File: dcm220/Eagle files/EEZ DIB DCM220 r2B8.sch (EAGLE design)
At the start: 244 parts, among them IC1 Si8662AB-B-IS1, IC10 MC33272ADR2G, IC11 LT3763EFE#PBF, IC12 MC33274ADR2G, IC13 LT3763EFE#PBF, IC2 TPS54060DGQ, IC3 Si8641AB-B-IS1, IC4 M24C32-WMN6P, IC5 LP2985-33DBVR, IC6 74HC2G04GW,125, IC7 N.C., IC8 STM32F373C8T6, IC9 TL431B, J1 4907, J2 571-0500, J3 571-0100, J4 571-0500, J5 571-0100, Q1 BSP716NH6327XTSA1, Q10 BSS84, Q2 NTD5867NLT4G, Q3 NTD5867NLT4G, Q4 BSS205NH6327XTSA1, Q5 BSS84, Q6 BSP716NH6327XTSA1, Q7 NTD5867NLT4G, Q8 NTD5867NLT4G, Q9 BSS205NH6327XTSA1, X1 39-30-1020, X2 77317-104-28LF, X3 N.C., X4 DS1024-2*5R0, Y1 LF XTAL026392

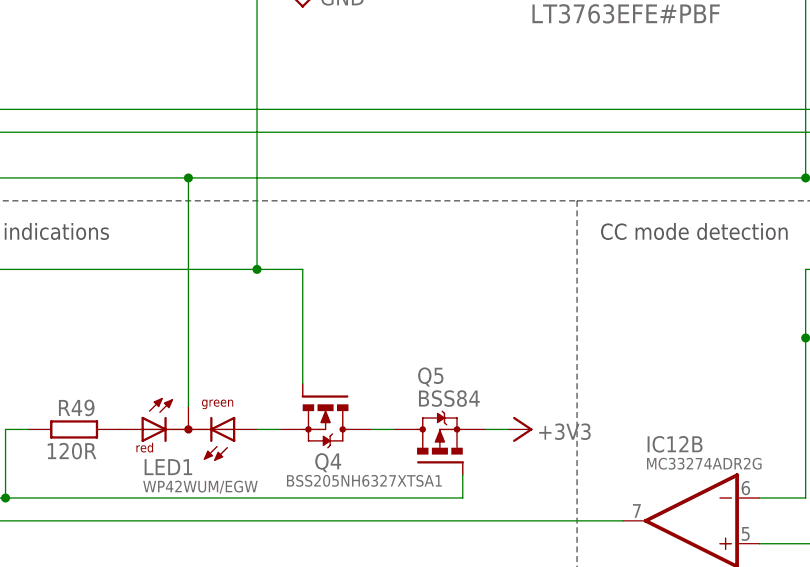
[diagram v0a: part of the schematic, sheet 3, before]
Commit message: DCM220 OE pull-down added
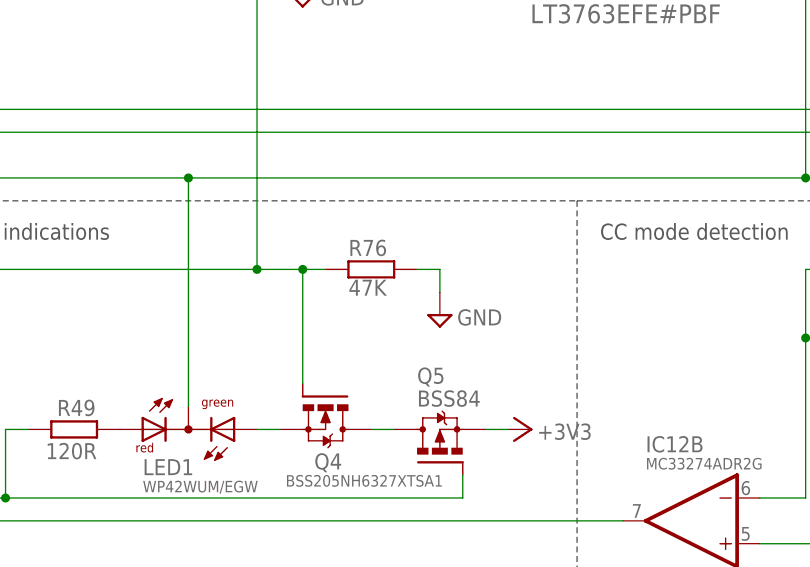
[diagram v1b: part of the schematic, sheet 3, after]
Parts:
- added R76, R77: 47K, rcl:R-EU_R0805
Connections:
- net GND: now also R76.2, R77.2
- net OE#1: now also R76.1
- net OE#2: now also R77.1
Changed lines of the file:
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@@
 <setting verticaltext="up"/>
 </settings>
-<grid distance="0.025" unitdist="inch" unit="inch" style="lines" multiple="4" display="no" altdistance="0.01" altunitdist="inch" altunit="inch"/>
+<grid distance="0.1" unitdist="inch" unit="inch" style="lines" multiple="1" display="no" altdistance="0.01" altunitdist="inch" altunit="inch"/>
 <layers>
 <layer number="1" name="Top" color="4" fill="1" visible="no" active="no"/>
@@
 <part name="+3V15" library="supply1" deviceset="+3V3" device=""/>
 <part name="U$3" library="OSHWA" deviceset="CERT" device="-SMALL" value="HR000002"/>
+<part name="R76" library="rcl" deviceset="R-EU_" device="R0805" value="47K"/>
+<part name="SUPPLY6" library="supply2" deviceset="GND" device=""/>
+<part name="R77" library="rcl" deviceset="R-EU_" device="R0805" value="47K"/>
+<part name="SUPPLY45" library="supply2" deviceset="GND" device=""/>
 </parts>
 <sheets>
@@
 <attribute name="VALUE" x="242.57" y="151.13" size="1.778" layer="96"/>
 </instance>
+<instance part="R76" gate="G$1" x="58.42" y="50.8" smashed="yes" rot="MR180">
+<attribute name="NAME" x="55.88" y="52.2986" size="1.778" layer="95"/>
+<attribute name="VALUE" x="55.88" y="49.657" size="1.778" layer="96" rot="MR180"/>
+</instance>
+<instance part="SUPPLY6" gate="GND" x="66.04" y="45.72" smashed="yes">
+<attribute name="VALUE" x="67.945" y="46.355" size="1.778" layer="96" rot="MR180"/>
+</instance>
 </instances>
 <busses>
@@
 <pinref part="SUPPLY44" gate="GND" pin="GND"/>
 </segment>
+<segment>
+<pinref part="R76" gate="G$1" pin="2"/>
+<wire x1="63.5" y1="50.8" x2="66.04" y2="50.8" width="0.1524" layer="91"/>
+<wire x1="66.04" y1="50.8" x2="66.04" y2="48.26" width="0.1524" layer="91"/>
+<pinref part="SUPPLY6" gate="GND" pin="GND"/>
+</segment>
 </net>
 <net name="OE#1" class="0">
@@
 <wire x1="45.72" y1="50.8" x2="50.8" y2="50.8" width="0.1524" layer="91"/>
 <wire x1="50.8" y1="50.8" x2="50.8" y2="38.1" width="0.1524" layer="91"/>
+<pinref part="R76" gate="G$1" pin="1"/>
+<wire x1="53.34" y1="50.8" x2="50.8" y2="50.8" width="0.1524" layer="91"/>
+<junction x="50.8" y="50.8"/>
 </segment>
 </net>
@@
 <attribute name="VALUE" x="113.284" y="159.639" size="1.778" layer="96" rot="MR180"/>
 </instance>
+<instance part="R77" gate="G$1" x="58.42" y="50.8" smashed="yes" rot="MR180">
+<attribute name="NAME" x="55.88" y="52.2986" size="1.778" layer="95"/>
+<attribute name="VALUE" x="55.88" y="49.657" size="1.778" layer="96" rot="MR180"/>
+</instance>
+<instance part="SUPPLY45" gate="GND" x="66.04" y="45.72" smashed="yes">
+<attribute name="VALUE" x="67.945" y="46.355" size="1.778" layer="96" rot="MR180"/>
+</instance>
 </instances>
 <busses>
@@
 <pinref part="SUPPLY19" gate="GND" pin="GND"/>
 </segment>
+<segment>
+<pinref part="R77" gate="G$1" pin="2"/>
+<wire x1="63.5" y1="50.8" x2="66.04" y2="50.8" width="0.1524" layer="91"/>
+<wire x1="66.04" y1="50.8" x2="66.04" y2="48.26" width="0.1524" layer="91"/>
+<pinref part="SUPPLY45" gate="GND" pin="GND"/>
+</segment>
 </net>
 <net name="N$28" class="0">
@@
 <wire x1="45.72" y1="137.16" x2="45.72" y2="50.8" width="0.1524" layer="91"/>
 <junction x="45.72" y="50.8"/>
+<wire x1="53.34" y1="50.8" x2="50.8" y2="50.8" width="0.1524" layer="91"/>
+<junction x="50.8" y="50.8"/>
+<pinref part="R77" gate="G$1" pin="1"/>
 </segment>
 </net>

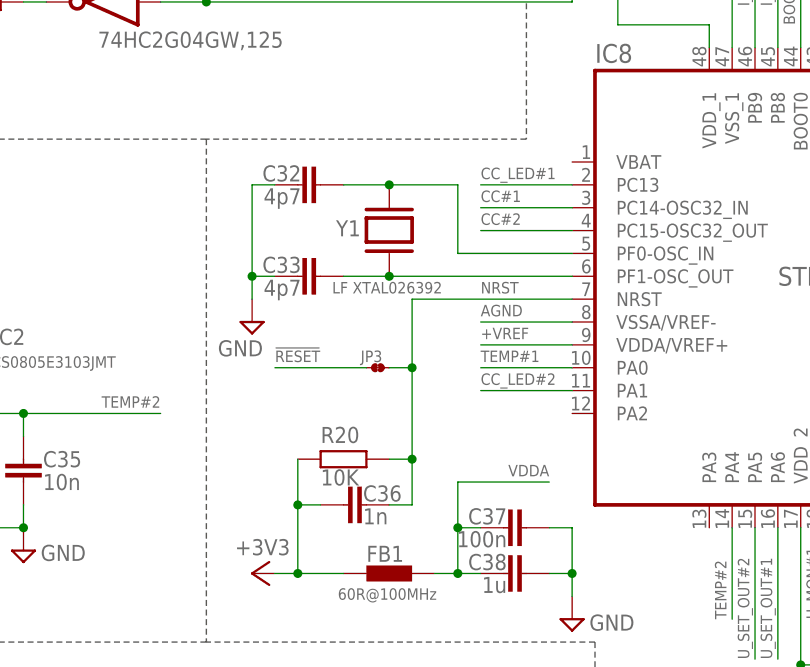
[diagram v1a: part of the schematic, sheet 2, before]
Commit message: DCM220 HSE removed
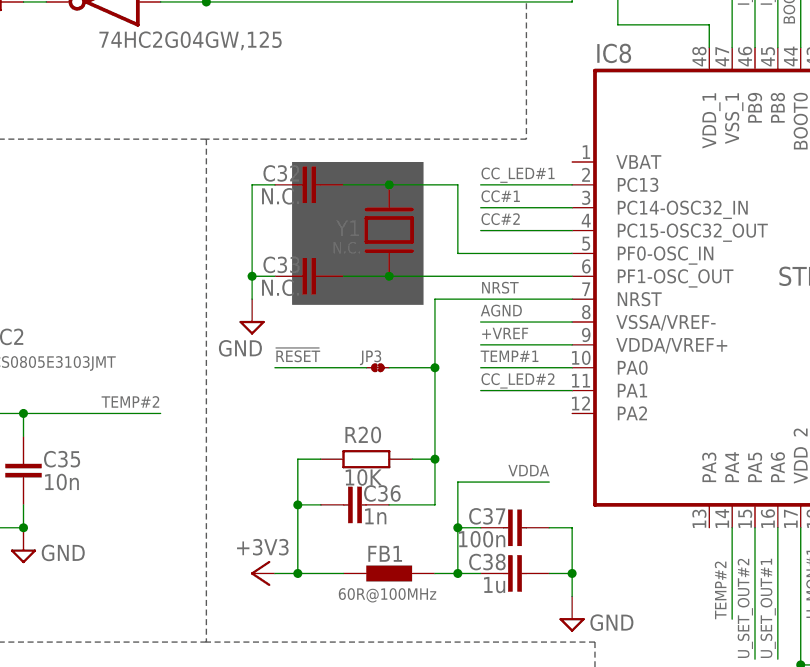
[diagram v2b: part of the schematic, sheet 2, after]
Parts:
- C32, C33: value 4p7 -> N.C.
- Y1: value LF XTAL026392 -> N.C.
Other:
- moved on the sheet: R20
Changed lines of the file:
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@@
 <part name="C62" library="EEZ_Lib1" deviceset="ECAP" device="5G_10.5MM" value="UVZ1E102MPD"/>
 <part name="C82" library="EEZ_Lib1" deviceset="ECAP" device="5G_10.5MM" value="UVZ1E102MPD"/>
-<part name="Y1" library="EEZ_Lib1" deviceset="XTAL" device="7.5X5.1-B" value="LF XTAL026392"/>
-<part name="C32" library="rcl" deviceset="C-EU" device="C0603" value="4p7"/>
-<part name="C33" library="rcl" deviceset="C-EU" device="C0603" value="4p7"/>
+<part name="Y1" library="EEZ_Lib1" deviceset="XTAL" device="7.5X5.1-B" value="N.C."/>
+<part name="C32" library="rcl" deviceset="C-EU" device="C0603" value="N.C."/>
+<part name="C33" library="rcl" deviceset="C-EU" device="C0603" value="N.C."/>
 <part name="SUPPLY49" library="supply2" deviceset="GND" device=""/>
 <part name="X4" library="EEZ_connectors" deviceset="SSW-105-02-T-D-RA" device="" value="DS1024-2*5R0"/>
@@
 <wire x1="208.28" y1="38.1" x2="208.28" y2="83.82" width="0.1524" layer="97" style="shortdash"/>
 <text x="210.82" y="78.74" size="1.778" layer="97">Voltage reference</text>
+<rectangle x1="90.805" y1="98.425" x2="105.41" y2="114.3" layer="97"/>
 </plain>
 <instances>
@@
 <instance part="Y1" gate="A" x="101.6" y="106.68" smashed="yes" rot="MR90">
 <attribute name="NAME" x="98.425" y="106.045" size="1.778" layer="95" rot="MR0"/>
-<attribute name="VALUE" x="95.25" y="100.965" size="1.27" layer="96" rot="MR180"/>
+<attribute name="VALUE" x="95.25" y="105.41" size="1.27" layer="96" rot="MR180"/>
 </instance>
 <instance part="C32" gate="G$1" x="91.44" y="111.76" smashed="yes" rot="R90">
@@
 <attribute name="NAME" x="98.425" y="92.075" size="1.27" layer="95"/>
 </instance>
-<instance part="R20" gate="G$1" x="96.52" y="81.28" smashed="yes" rot="MR180">
-<attribute name="NAME" x="93.98" y="84.8614" size="1.778" layer="95" rot="MR180"/>
-<attribute name="VALUE" x="93.98" y="80.137" size="1.778" layer="96" rot="MR180"/>
+<instance part="R20" gate="G$1" x="99.06" y="81.28" smashed="yes" rot="MR180">
+<attribute name="NAME" x="96.52" y="84.8614" size="1.778" layer="95" rot="MR180"/>
+<attribute name="VALUE" x="96.52" y="80.137" size="1.778" layer="96" rot="MR180"/>
 </instance>
 <instance part="C36" gate="G$1" x="99.06" y="76.2" smashed="yes" rot="MR90">
@@
 <junction x="91.44" y="68.58"/>
 <pinref part="R20" gate="G$1" pin="1"/>
+<junction x="91.44" y="76.2"/>
+<wire x1="93.98" y1="81.28" x2="91.44" y2="81.28" width="0.1524" layer="91"/>
 <wire x1="91.44" y1="81.28" x2="91.44" y2="76.2" width="0.1524" layer="91"/>
-<junction x="91.44" y="76.2"/>
 </segment>
 <segment>
@@
 <pinref part="IC8" gate="G$1" pin="NRST"/>
 <pinref part="JP3" gate="G$1" pin="2"/>
-<wire x1="121.92" y1="99.06" x2="104.14" y2="99.06" width="0.1524" layer="91"/>
-<wire x1="104.14" y1="99.06" x2="104.14" y2="91.44" width="0.1524" layer="91"/>
-<wire x1="104.14" y1="91.44" x2="101.6" y2="91.44" width="0.1524" layer="91"/>
+<wire x1="121.92" y1="99.06" x2="106.68" y2="99.06" width="0.1524" layer="91"/>
+<wire x1="106.68" y1="99.06" x2="106.68" y2="91.44" width="0.1524" layer="91"/>
+<wire x1="106.68" y1="91.44" x2="101.6" y2="91.44" width="0.1524" layer="91"/>
 <label x="111.76" y="99.695" size="1.27" layer="102"/>
 <pinref part="R20" gate="G$1" pin="2"/>
-<wire x1="101.6" y1="81.28" x2="104.14" y2="81.28" width="0.1524" layer="91"/>
-<wire x1="104.14" y1="81.28" x2="104.14" y2="91.44" width="0.1524" layer="91"/>
-<junction x="104.14" y="91.44"/>
+<wire x1="104.14" y1="81.28" x2="106.68" y2="81.28" width="0.1524" layer="91"/>
+<wire x1="106.68" y1="81.28" x2="106.68" y2="91.44" width="0.1524" layer="91"/>
+<junction x="106.68" y="91.44"/>
 <pinref part="C36" gate="G$1" pin="1"/>
-<wire x1="101.6" y1="76.2" x2="104.14" y2="76.2" width="0.1524" layer="91"/>
-<wire x1="104.14" y1="76.2" x2="104.14" y2="81.28" width="0.1524" layer="91"/>
-<junction x="104.14" y="81.28"/>
-</segment>
-<segment>
+<wire x1="101.6" y1="76.2" x2="106.68" y2="76.2" width="0.1524" layer="91"/>
+<wire x1="106.68" y1="76.2" x2="106.68" y2="81.28" width="0.1524" layer="91"/>
+<junction x="106.68" y="81.28"/>
+</segment>
+<segment>

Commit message: ULVO levels update for power modules
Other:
- note added: "UVLO off: +26.5 V UVLO on: +27.5 V"
- note removed: "UVLO off: +33 V UVLO on: +38 V"
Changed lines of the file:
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@@
 <text x="247.65" y="132.715" size="1.4224" layer="101">28 UART_TX</text>
 <wire x1="71.12" y1="2.54" x2="71.12" y2="60.96" width="0.1524" layer="97" style="shortdash"/>
-<text x="36.83" y="113.665" size="1.778" layer="103">UVLO off: +33 V
-UVLO on: +38 V</text>
+<text x="36.83" y="113.665" size="1.778" layer="103">UVLO off: +26.5 V
+UVLO on: +27.5 V</text>
 <text x="76.2" y="58.42" size="1.778" layer="97" rot="MR180">+3V3 LDO</text>
 <text x="193.675" y="81.28" size="1.27" layer="103">Max. transfer speed is 1MBit/s</text>

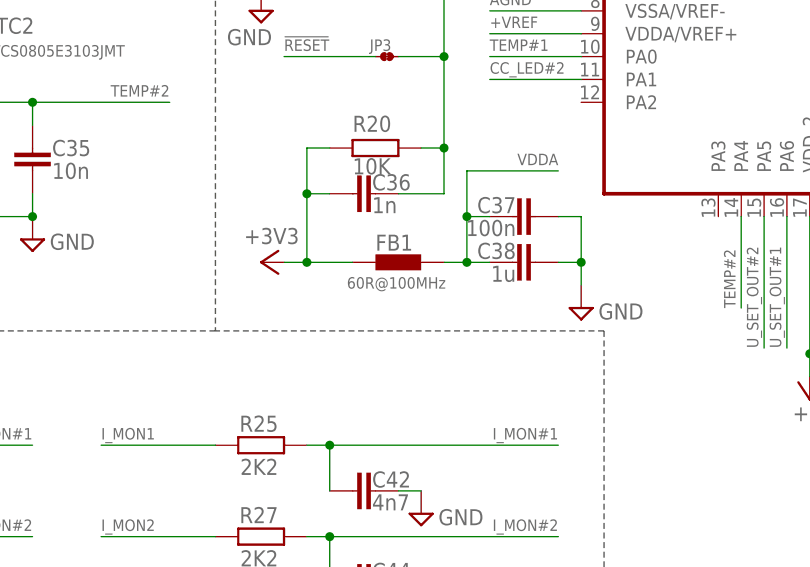
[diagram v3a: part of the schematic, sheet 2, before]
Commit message: FB values updated for DCP405 and DCM220
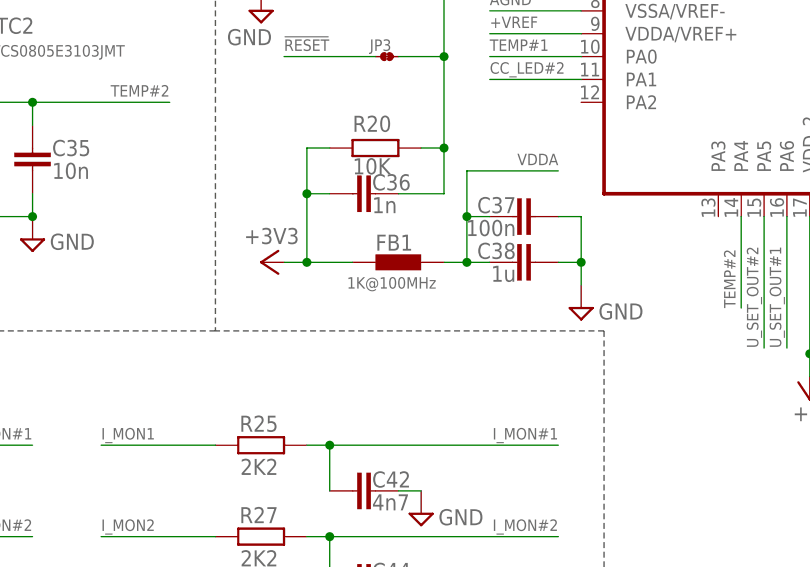
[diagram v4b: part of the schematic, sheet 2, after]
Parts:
- FB1: value 60R@100MHz -> 1K@100MHz
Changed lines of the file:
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@@
 <part name="R15" library="rcl" deviceset="R-EU_" device="R0805" value="10K"/>
 <part name="SUPPLY63" library="supply2" deviceset="GND" device=""/>
-<part name="FB1" library="EEZ_Lib1" deviceset="FERRITE_BEAD" device="0603" value="60R@100MHz"/>
+<part name="FB1" library="EEZ_Lib1" deviceset="FERRITE_BEAD" device="0603" value="1K@100MHz"/>
 <part name="+3V7" library="supply1" deviceset="+3V3" device=""/>
 <part name="C37" library="rcl" deviceset="C-EU" device="C0603" value="100n"/>
